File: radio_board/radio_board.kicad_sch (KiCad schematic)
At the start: 95 parts, among them J1 3.3v, J2 GND, J3 RESET, J4 SWDCLK, J5 SWDIO, Q1 2N7002K, SW2 RKB2SJG250SMTRLFS, SW3 MSK12C02, U1 FSC-BT1036C, U2 TP4057, U3 XB5352A, U5 S2B-PH-K-S(LF)(SN), U6 TLV75533PDBVR, U7 LMV321, U8 STM32G030F6P6TR

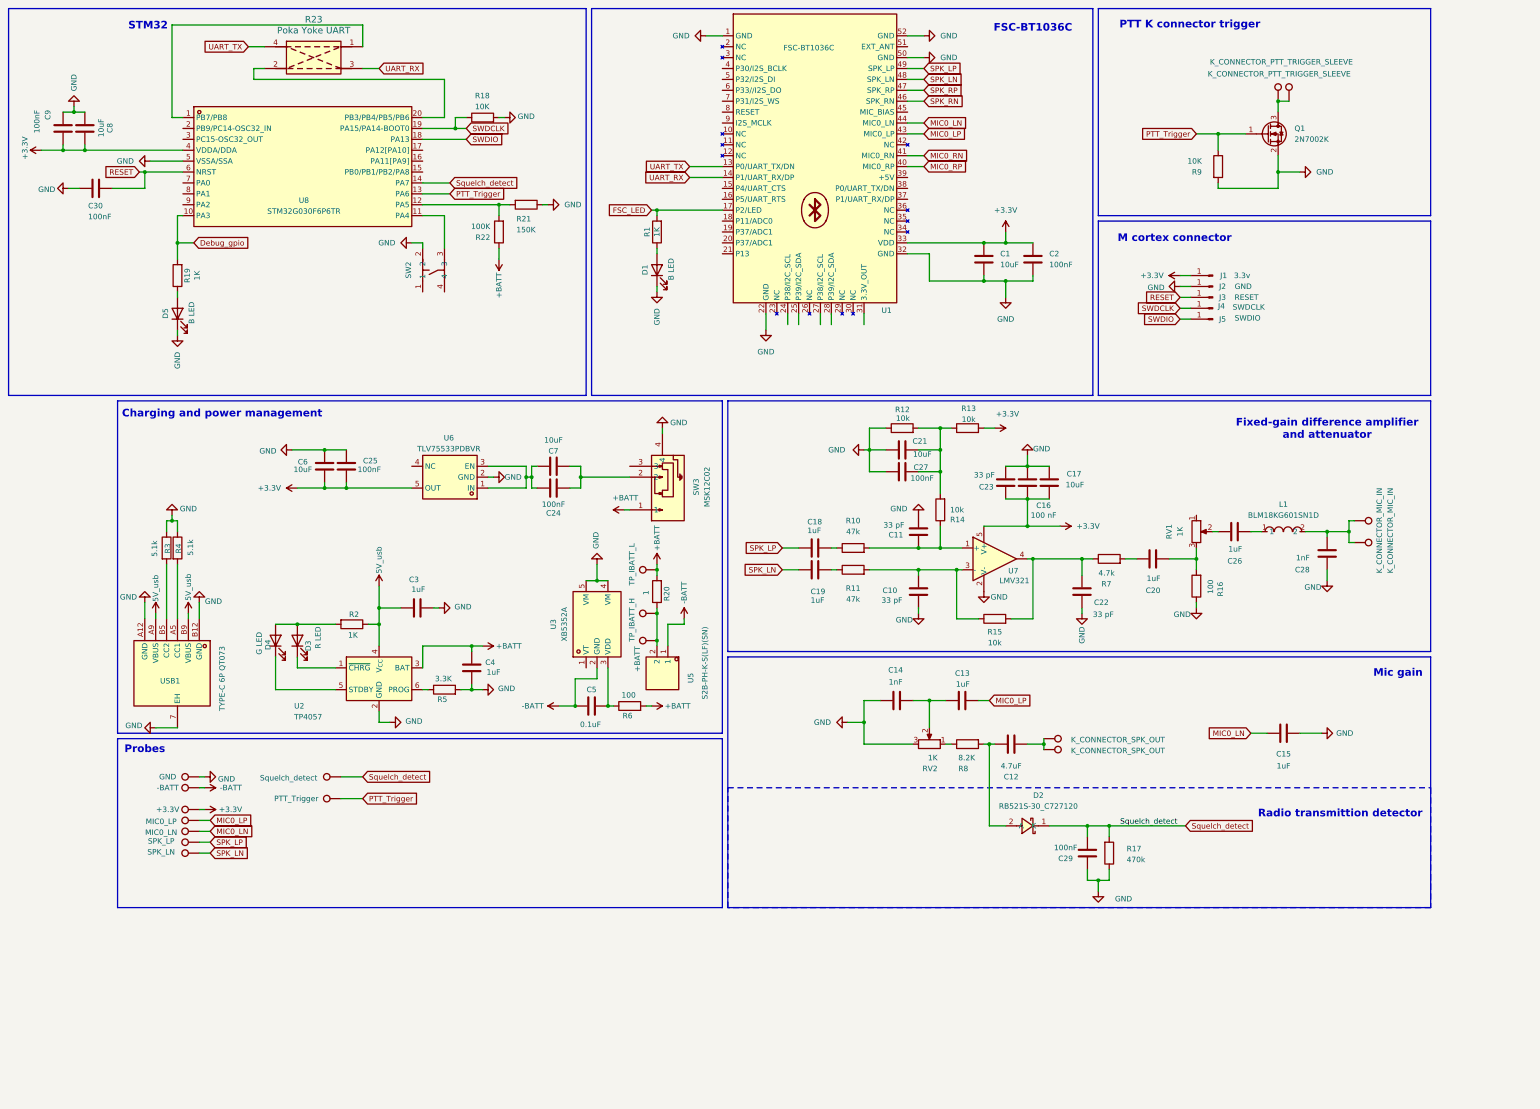
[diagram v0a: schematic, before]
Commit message: [Feature] Cleaned up PCB and schematics. Add logo, checked schematic, layout and wiring
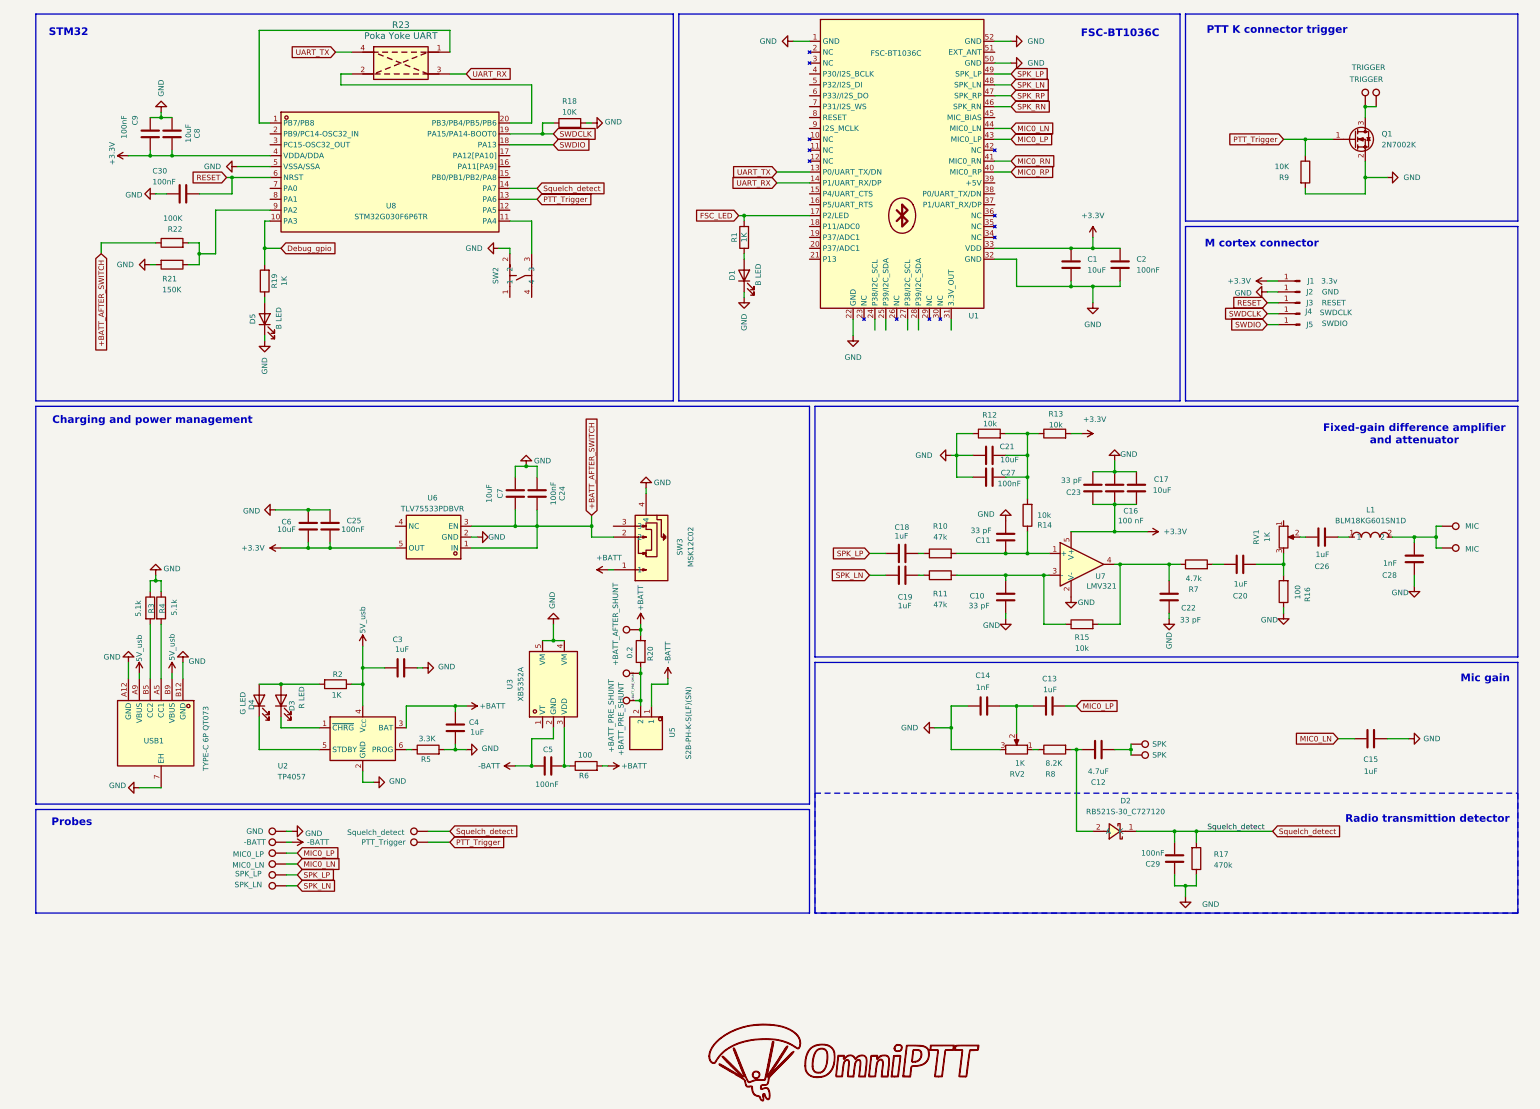
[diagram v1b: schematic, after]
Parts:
- removed TP41: +3.3V, TestPoint:TestPoint_THTPad_D2.0mm_Drill1.0mm, symbol Connector:TestPoint
- C14, C15: footprint Capacitor_SMD:C_0603_1608Metric_Pad1.08x0.95mm_HandSolder -> Resistor_SMD:R_0603_1608Metric_Pad0.98x0.95mm_HandSolder
- C5: value 0.1uF -> 100nF
- R20: value 1 -> 0.2
- TP1: value TP_IBATT_H -> +BATT_PRE_SHUNT
- TP14, TP43: value K_CONNECTOR_PTT_TRIGGER_SLEEVE -> TRIGGER
- TP20, TP45: value K_CONNECTOR_SPK_OUT -> SPK
- TP3: value TP_IBATT_L -> +BATT_AFTER_SHUNT
- TP47: value +BATT -> +BATT_PRE_SHUNT
- TP50, TP51: value K_CONNECTOR_MIC_IN -> MIC
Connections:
- net +BATT: no longer R22.1
- net GND: now also C24.1, C7.1, R21.2; no longer R21.1
- net at U8.9 (PA2): now also R21.1, R22.2
- net +BATT_PRE_SHUNT: now reaches R20.1, TP1.1, TP47.1, U5.2
- net +BATT_AFTER_SWITCH: now reaches C24.2, C7.2, U6.1 (IN), U6.3 (EN)
- net +BATT_AFTER_SWITCH: now also R22.1, SW3.2
- now unconnected: U8.12 (PA5)
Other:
- moved on the sheet: C1, C10, C11, C12, C13, C14, C15, C16, C17, C18, C19, C2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

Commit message: [Milestone] Last commit before pourchasing v2
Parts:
- removed C23: 33 pF, Resistor_SMD:R_0603_1608Metric_Pad0.98x0.95mm_HandSolder, symbol Device:C
- added C31: 100pF, Resistor_SMD:R_0603_1608Metric_Pad0.98x0.95mm_HandSolder, symbol Device:C
- added L2: BLM18KG601SN1D, PTT_Project_library:L0603, symbol PTT_Project_library:BLM18KG601SN1D
- C1, C12, C13, C15, C17, C18, C19, C2, C20, C21, C24, C25, C26, C27, C29, C3, C30, C4, C5, C8, C9, D1, D3, D4, D5, Q1, R12, R13, R14, R15, R16, R23, R3, R4, R6, SW2, SW3, TP1, TP14, TP2, TP3, TP33, TP34, TP38, TP44, TP45, TP49, TP5, TP50, U1, U2, U3, U5, USB1: now left out of the parts list
- C10, C11, C22: value 33 pF -> 33pF; LCSC Part (none) -> C107047
- C14: value 1nF -> 47nF; LCSC Part (none) -> C107093
- C16: value 100 nF -> 100nF; now left out of the parts list
- C28: value 1nF -> 100pF; LCSC Part (none) -> C14665
- C6, C7: value 10uF -> 22uF; footprint Resistor_SMD:R_0603_1608Metric_Pad0.98x0.95mm_HandSolder -> Resistor_SMD:R_0805_2012Metric_Pad1.20x1.40mm_HandSolder; LCSC Part (none) -> C602037
- J1, J2, J3, J4, J5: footprint Connector_PinSocket_2.54mm:PinSocket_1x01_P2.54mm_Vertical -> Connector_PinHeader_2.54mm:PinHeader_1x01_P2.54mm_Vertical; now left out of the parts list
- R1, R19, R2, RV1, RV2: value 1K -> 1k; now left out of the parts list
- R10, R11: LCSC Part (none) -> C105579
- R17: LCSC Part (none) -> C114622
- R18, R9: value 10K -> 10k; now left out of the parts list
- R20: LCSC Part (none) -> C723543
- R21: value 150K -> 150k; LCSC Part (none) -> C114660
- R22: value 100K -> 100k; LCSC Part (none) -> C14675
- R5: value 3.3K -> 3.3k; now left out of the parts list
- R7: LCSC Part (none) -> C99782
- R8: value 8.2K -> 8.2k; now left out of the parts list
- TP20, TP43, TP51: footprint TestPoint:TestPoint_Pad_D3.0mm -> TestPoint:TestPoint_THTPad_D2.0mm_Drill1.0mm; now left out of the parts list
- TP47, TP6: footprint TestPoint:TestPoint_Pad_D2.5mm -> TestPoint:TestPoint_THTPad_D2.0mm_Drill1.0mm; now left out of the parts list
- U7: LCSC Part (none) -> C7972
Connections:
- net GND: now also C31.1
- net at TP20.1, TP45.1: now also C31.2, L2.2; no longer C12.1
- new net: C12.1, L2.1
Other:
- moved on the sheet: C16, C17

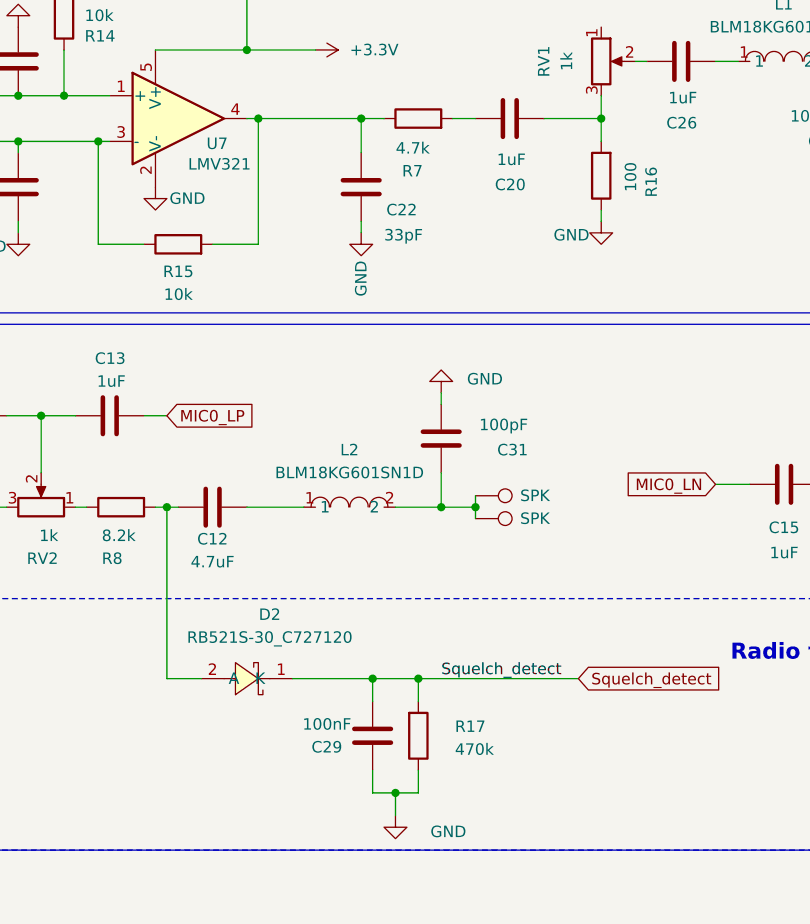
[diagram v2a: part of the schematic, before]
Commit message: [Fix] Changed a resistor value to lower attenuation of baofeng MIC in
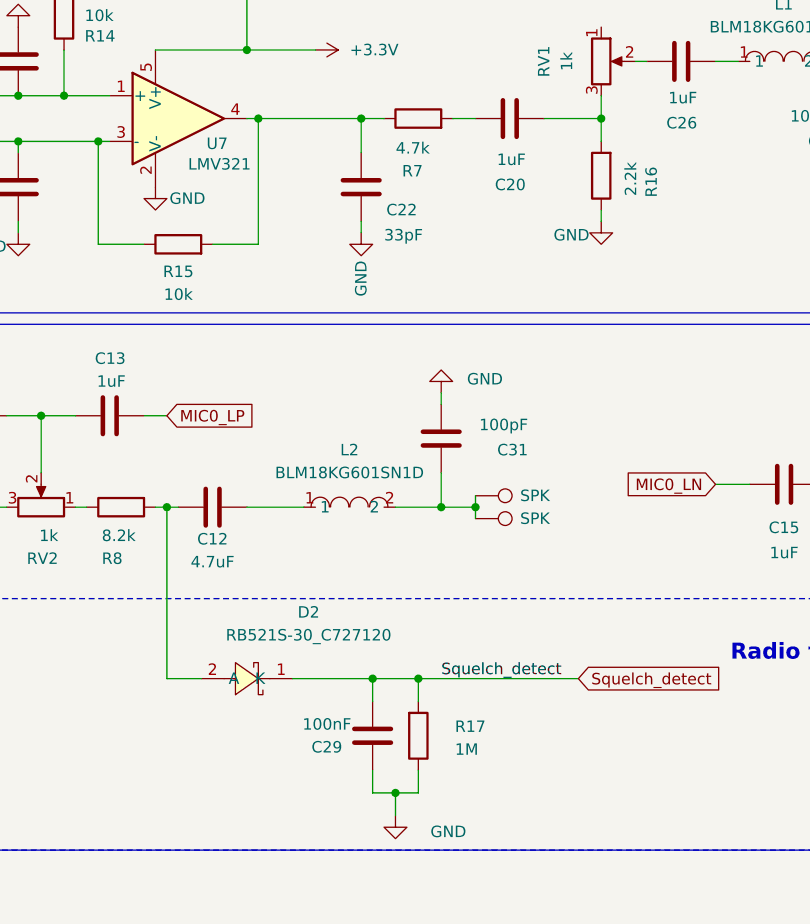
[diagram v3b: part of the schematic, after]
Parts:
- R16: value 100 -> 2.2k
- R17: value 470k -> 1M
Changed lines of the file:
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@@
 	)
 	(junction
+		(at 261.62 185.42)
+		(diameter 0)
+		(color 0 0 0 0)
+	)
+	(junction
 		(at 328.93 52.07)
 		(diameter 0)
@@
 	)
 	(junction
-		(at 261.62 185.42)
-		(diameter 0)
-		(color 0 0 0 0)
-	)
-	(junction
 		(at 76.2 170.18)
 		(diameter 0)
@@
 	(wire
 		(pts
-			(xy 261.62 185.42) (xy 262.89 185.42)
-		)
-		(stroke
-			(width 0)
-			(type default)
-		)
-	)
-	(wire
-		(pts
 			(xy 209.55 85.09) (xy 209.55 88.9)
 		)
@@
 	(wire
 		(pts
+			(xy 261.62 185.42) (xy 261.62 204.47)
+		)
+		(stroke
+			(width 0)
+			(type default)
+		)
+	)
+	(wire
+		(pts
 			(xy 335.28 135.89) (xy 340.36 135.89)
 		)
@@
 	(wire
 		(pts
-			(xy 261.62 204.47) (xy 261.62 185.42)
-		)
-		(stroke
-			(width 0)
-			(type default)
-		)
-	)
-	(wire
-		(pts
 			(xy 134.62 30.48) (xy 90.17 30.48)
 		)
@@
 	(wire
 		(pts
+			(xy 261.62 185.42) (xy 262.89 185.42)
+		)
+		(stroke
+			(width 0)
+			(type default)
+		)
+	)
+	(wire
+		(pts
 			(xy 306.07 76.2) (xy 308.61 76.2)
 		)
@@
 			)
 		)
-		(property "Value" "100"
+		(property "Value" "2.2k"
 			(at 313.182 147.066 90)
 			(effects
@@
 			)
 		)
-		(property "Value" "470k"
+		(property "Value" "1M"
 			(at 293.624 212.344 0)
 			(effects
@@
 		(dnp no)
 		(property "Reference" "D2"
-			(at 273.05 197.358 0)
+			(at 277.368 197.104 0)
 			(effects
 				(font
@@
 		)
 		(property "Value" "RB521S-30_C727120"
-			(at 273.05 199.898 0)
+			(at 277.368 199.644 0)
 			(effects
 				(font
